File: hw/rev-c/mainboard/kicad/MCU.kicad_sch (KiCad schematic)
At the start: 34 parts, among them J23 MENU, SW4 RUN, SW5 MENU, U21 RP2040, Y1 12 MHz

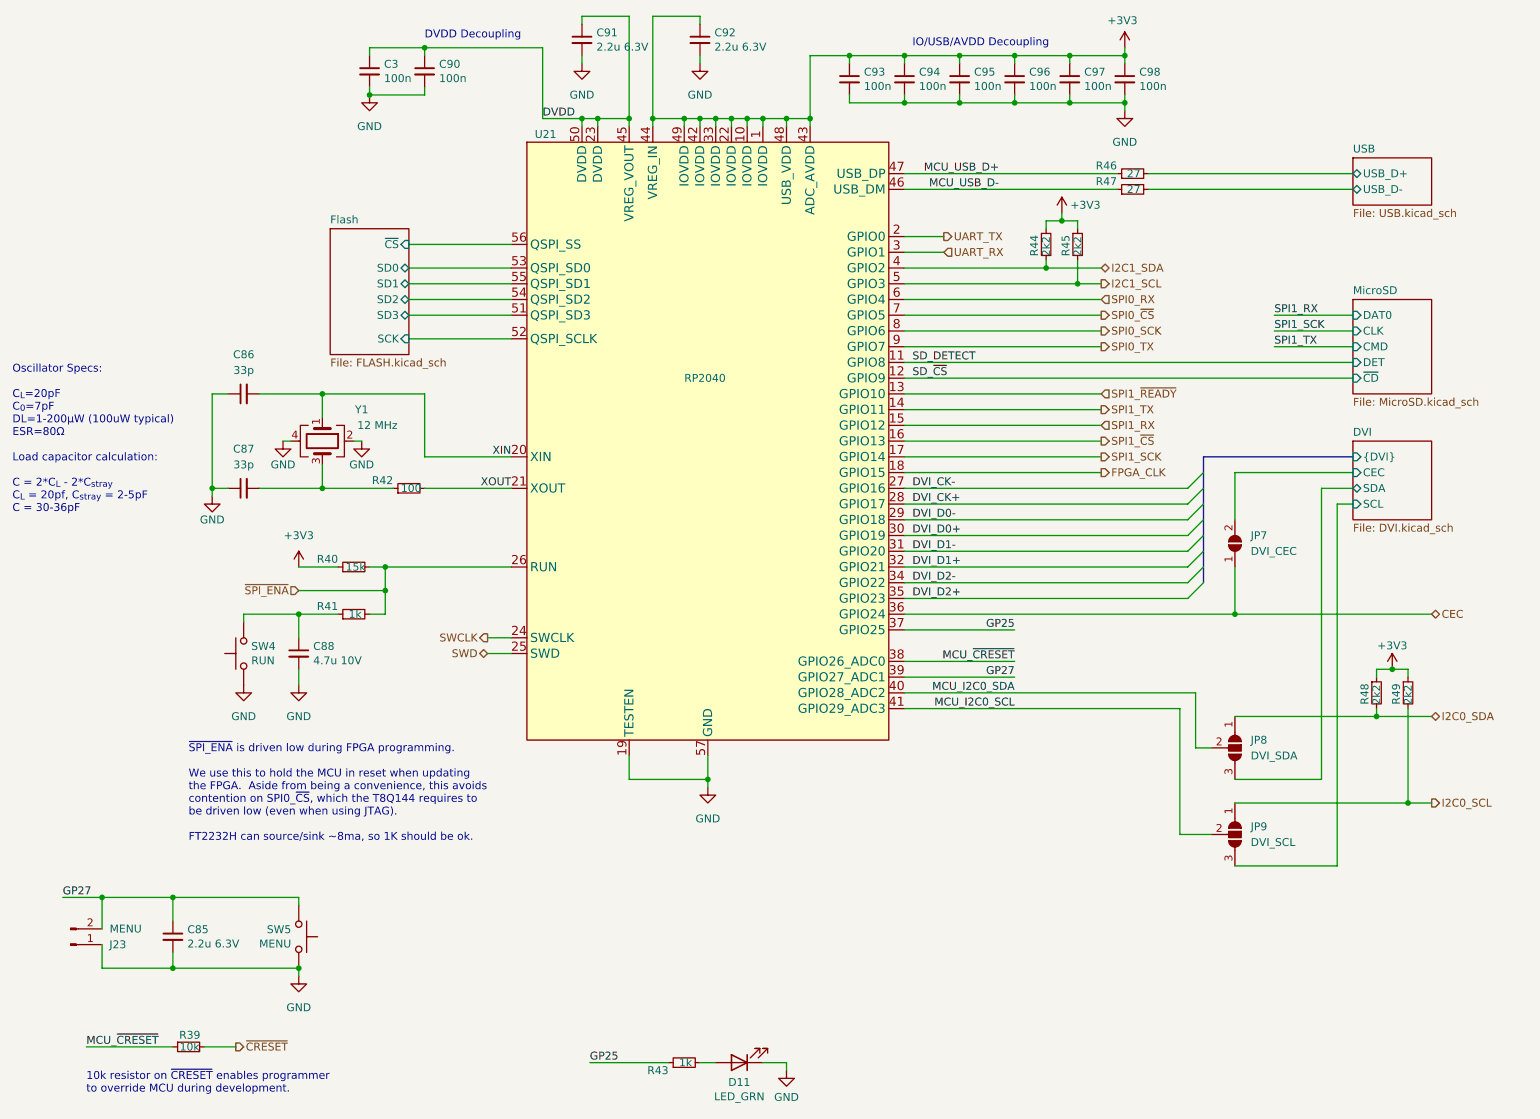
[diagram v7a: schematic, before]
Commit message: hw: routing touchups, killer poke mitigation
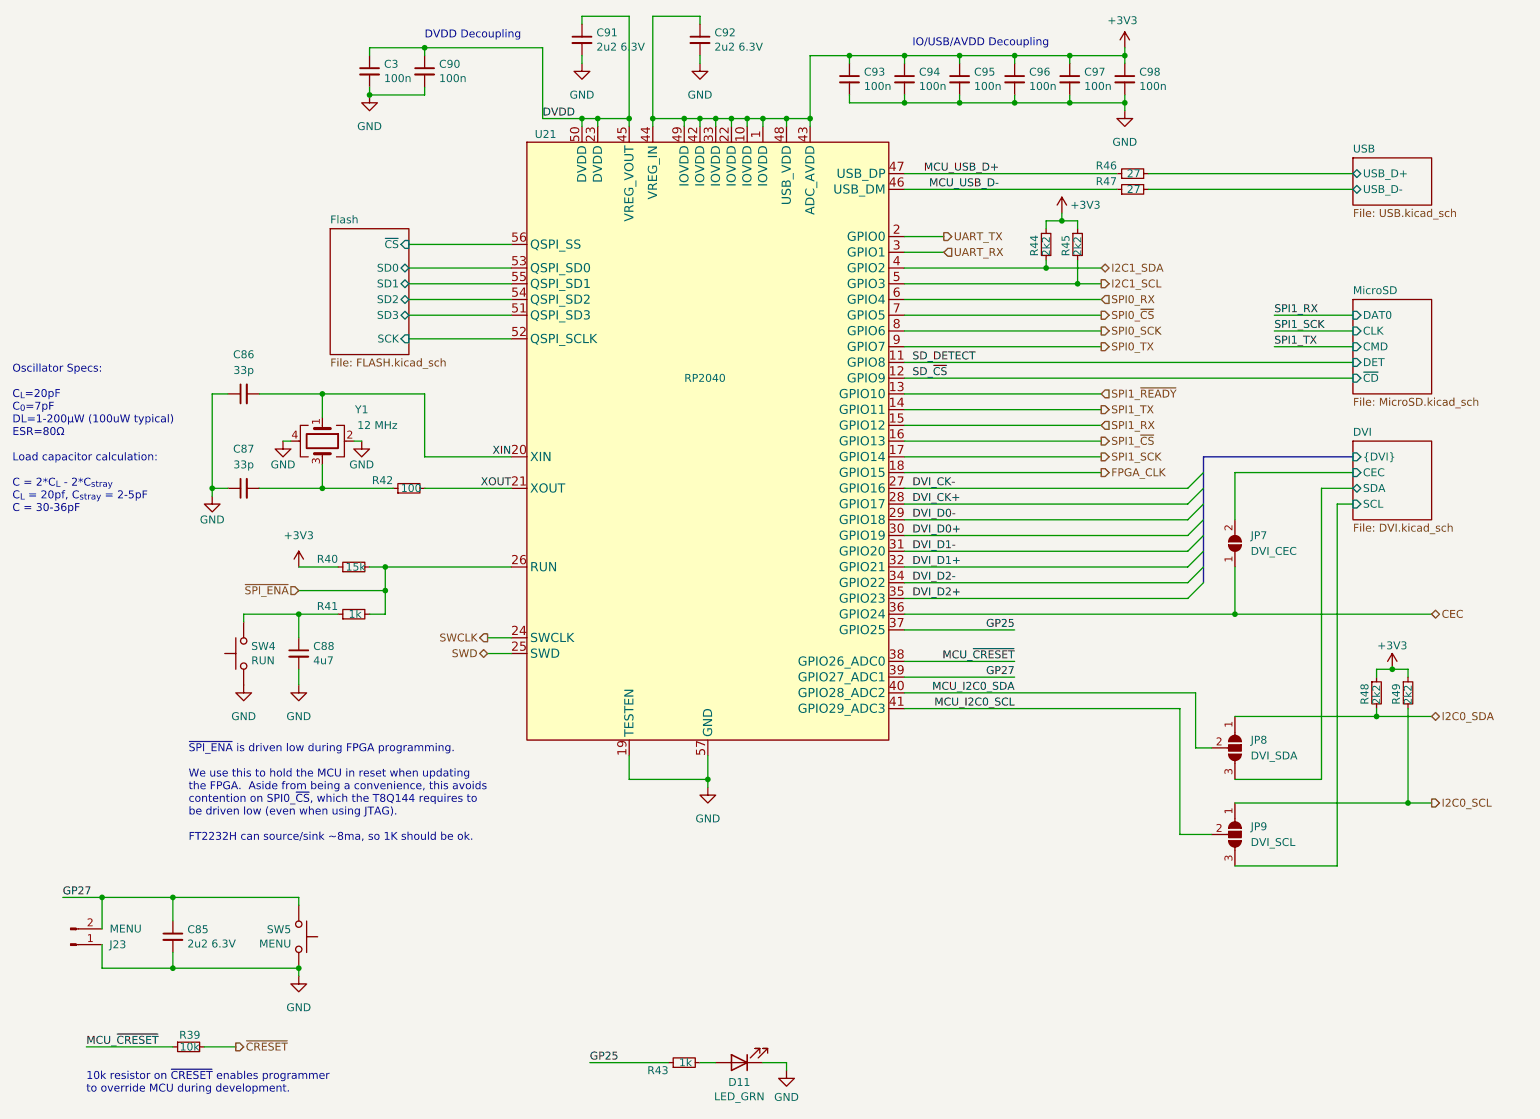
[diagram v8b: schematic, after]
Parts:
- C85, C91, C92: value 2.2u 6.3V -> 2u2 6.3V
- C88: value 4.7u 10V -> 4u7; LCSC C23733 -> C1538
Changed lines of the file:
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@@
 			)
 		)
-		(property "Value" "2.2u 6.3V"
+		(property "Value" "2u2 6.3V"
 			(at 129.3368 24.003 0)
 			(effects
@@
 			)
 		)
-		(property "Value" "2.2u 6.3V"
+		(property "Value" "2u2 6.3V"
 			(at 110.2868 24.003 0)
 			(effects
@@
 			)
 		)
-		(property "Value" "4.7u 10V"
+		(property "Value" "4u7"
 			(at 64.5668 123.063 0)
 			(effects
@@
 			)
 		)
-		(property "Datasheet" "https://product.samsungsem.com/mlcc/CL05A475MP5NRN.do"
+		(property "Datasheet" "https://www.lcsc.com/datasheet/lcsc_datasheet_2304140030_FH--Guangdong-Fenghua-Advanced-Tech-0402B472K500NT_C1538.pdf"
 			(at 62.23 121.92 0)
 			(effects
@@
 			)
 		)
-		(property "LCSC" "C23733"
+		(property "LCSC" "C1538"
 			(at 62.23 121.92 0)
 			(effects
@@
 			)
 		)
-		(property "Value" "2.2u 6.3V"
+		(property "Value" "2u2 6.3V"
 			(at 44.2468 168.783 0)
 			(effects
